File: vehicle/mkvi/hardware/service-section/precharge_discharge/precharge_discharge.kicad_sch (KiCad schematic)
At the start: 13 parts, among them J1 MicroFit_VT_5x1, J2 Automotive_M.2_Edge_Connector, K1 G2RG-2A-X_DC12, K2 3350-4275-126, Q1 SSM3K333R

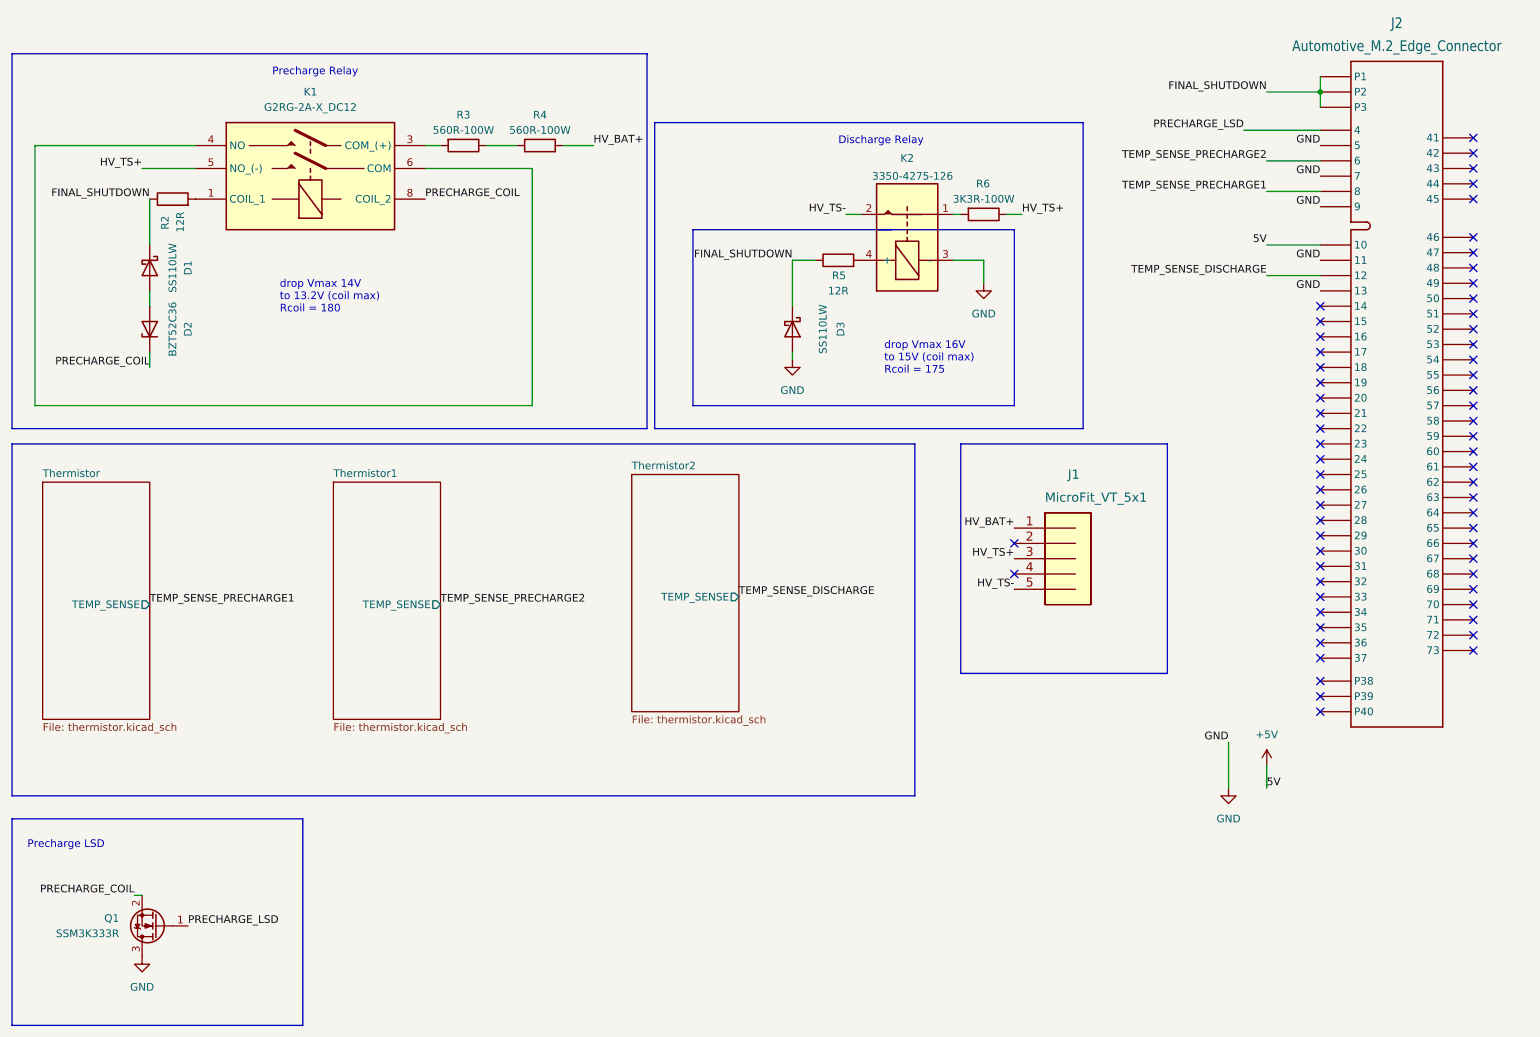
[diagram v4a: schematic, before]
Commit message: V3. Precharge_Discharge PCB Layout
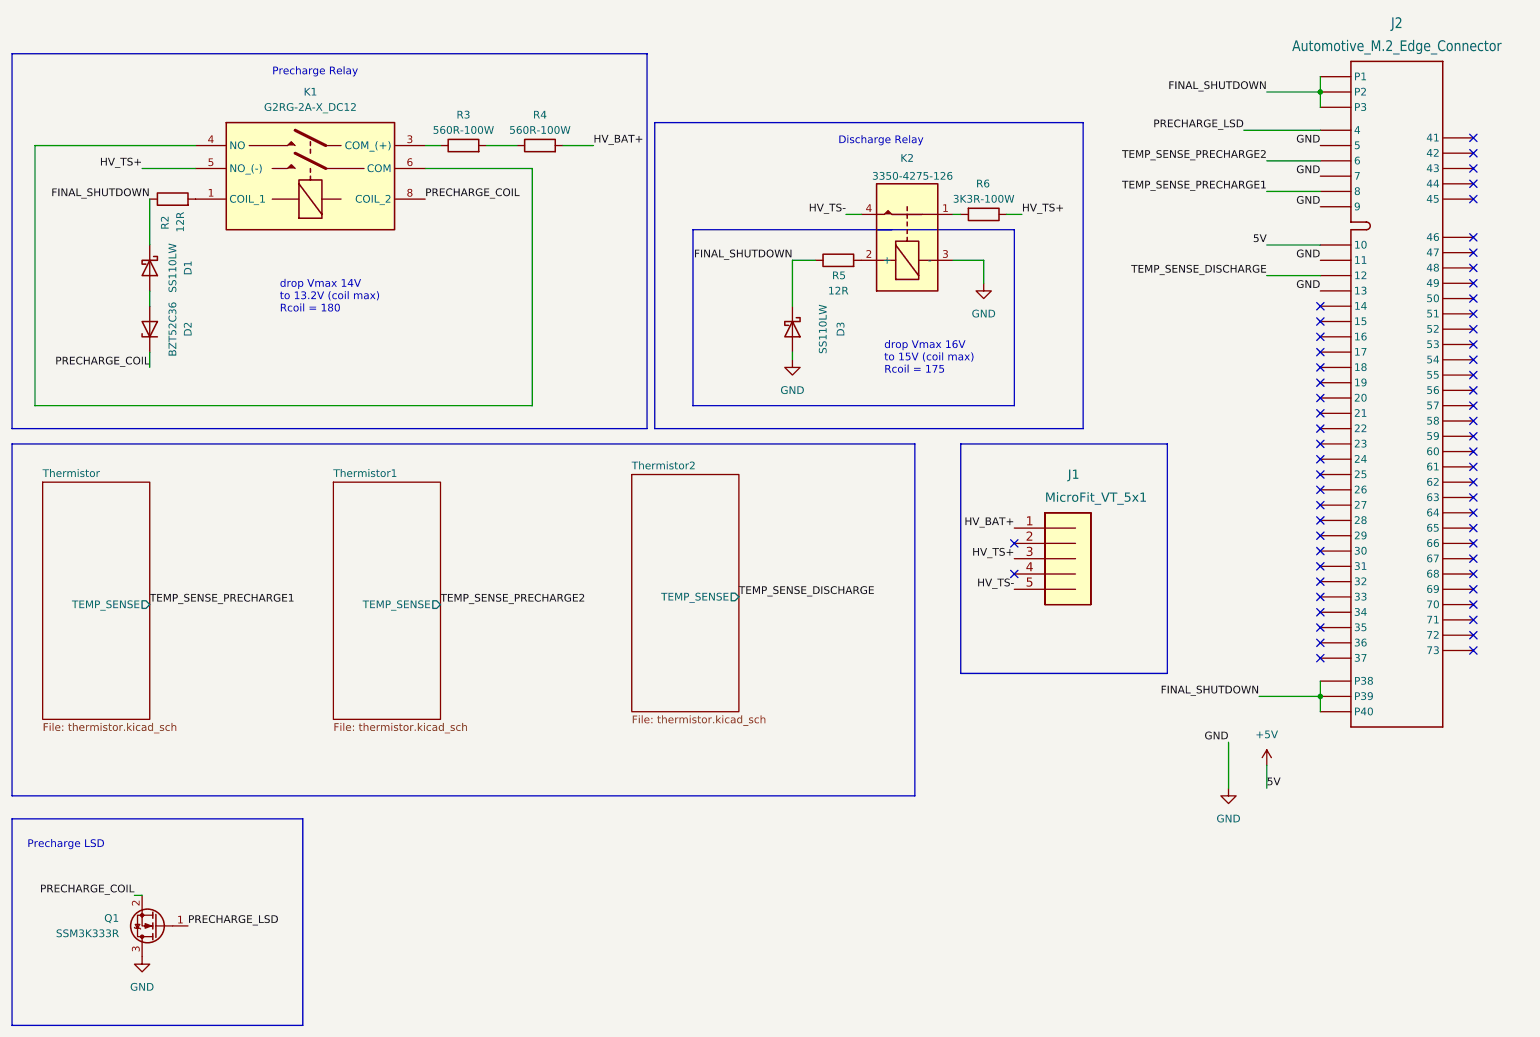
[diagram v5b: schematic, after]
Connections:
- net FINAL_SHUTDOWN: now also J2.P38, J2.P39, J2.P40
- net HV_TS-: now also K2.4; no longer K2.2
- net at K1.3 (COM_(+)): now also R3.1; no longer R3.2
- net at R5.2: now also K2.2 (+); no longer K2.4 (+)
- net at R4.1: now also R3.2; no longer R3.1
- no-connect marks 62 -> 59
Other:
- moved on the sheet: R3

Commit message: Implmeneted Requested Changes
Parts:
- added R1: R_10K, footprints:R_0805_OEM, symbol formula:R_10K
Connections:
- net GND: now also Q1.2 (S), R1.2; no longer Q1.3 (D)
- net PRECHARGE_COIL: now also Q1.3 (D); no longer Q1.2 (S)
- net PRECHARGE_LSD: now also R1.1
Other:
- moved on the sheet: Q1
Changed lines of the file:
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@@
+    (stroke (width 0) (type default) (color 0 0 0 0))
+  )
+  (wire (pts (xy 44.45 167.64) (xy 44.45 168.91))
     (stroke (width 0) (type default) (color 0 0 0 0))
   )
@@
     (stroke (width 0) (type default) (color 0 0 0 0))
   )
-  (wire (pts (xy 45.72 165.1) (xy 46.99 165.1))
+  (wire (pts (xy 50.8 162.56) (xy 52.07 162.56))
     (stroke (width 0) (type default) (color 0 0 0 0))
   )
@@
     (stroke (width 0) (type default) (color 0 0 0 0))
   )
+  (wire (pts (xy 52.07 176.53) (xy 52.07 172.72))
+    (stroke (width 0) (type default) (color 0 0 0 0))
+  )
   (polyline (pts (xy 73.66 152.4) (xy 25.4 152.4))
     (stroke (width 0) (type default) (color 0 0 0 0))
@@
     (effects (font (size 1.27 1.27)) (justify right bottom))
   )
-  (label "PRECHARGE_LSD" (at 54.61 170.18 0)
-    (effects (font (size 1.27 1.27)) (justify left bottom))
+  (label "PRECHARGE_LSD" (at 44.45 167.64 180)
+    (effects (font (size 1.27 1.27)) (justify right bottom))
   )
   (label "FINAL_SHUTDOWN" (at 48.26 49.53 180)
@@
     (effects (font (size 1.27 1.27)) (justify right bottom))
   )
-  (label "PRECHARGE_COIL" (at 45.72 165.1 180)
+  (label "PRECHARGE_COIL" (at 50.8 162.56 180)
     (effects (font (size 1.27 1.27)) (justify right bottom))
   )
@@
     (pin "2")
   )
-  (symbol (lib_id "power:GND") (at 46.99 175.26 0) (unit 1)
+  (symbol (lib_id "power:GND") (at 52.07 176.53 0) (unit 1)
     (in_bom yes) (on_board yes) (fields_autoplaced)
-    (property "Reference" "#PWR?" (id 0) (at 46.99 181.61 0)
-      (effects (font (size 1.27 1.27)) hide)
-    )
-    (property "Value" "GND" (id 1) (at 46.99 180.34 0))
-    (property "Footprint" "" (id 2) (at 46.99 175.26 0)
-      (effects (font (size 1.27 1.27)) hide)
-    )
-    (property "Datasheet" "" (id 3) (at 46.99 175.26 0)
+    (property "Reference" "#PWR?" (id 0) (at 52.07 182.88 0)
+      (effects (font (size 1.27 1.27)) hide)
+    )
+    (property "Value" "GND" (id 1) (at 52.07 181.61 0))
+    (property "Footprint" "" (id 2) (at 52.07 176.53 0)
+      (effects (font (size 1.27 1.27)) hide)
+    )
+    (property "Datasheet" "" (id 3) (at 52.07 176.53 0)
       (effects (font (size 1.27 1.27)) hide)
     )
@@
     (pin "1")
   )
-  (symbol (lib_id "OEM:SSM3K333R") (at 49.53 170.18 180) (unit 1)
+  (symbol (lib_id "OEM:SSM3K333R") (at 49.53 167.64 0) (unit 1)
     (in_bom yes) (on_board yes) (fields_autoplaced)
-    (property "Reference" "Q1" (id 0) (at 43.18 168.9099 0)
+    (property "Reference" "Q1" (id 0) (at 55.88 166.3699 0)
       (effects (font (size 1.27 1.27)) (justify left))
     )
-    (property "Value" "SSM3K333R" (id 1) (at 43.18 171.4499 0)
+    (property "Value" "SSM3K333R" (id 1) (at 55.88 168.9099 0)
       (effects (font (size 1.27 1.27)) (justify left))
     )
-    (property "Footprint" "OEM:SOT-23F" (id 2) (at 44.45 172.72 0)
-      (effects (font (size 1.27 1.27)) hide)
-    )
-    (property "Datasheet" "https://drive.google.com/file/d/1BgDITdtTCIIJgSi-AIzORLljOfl6uFKQ/view?usp=share_link" (id 3) (at 49.53 170.18 0)
-      (effects (font (size 1.27 1.27)) hide)
-    )
-    (property "MPN" "SSM3K333R,LF" (id 4) (at 43.18 172.7199 0)
+    (property "Footprint" "OEM:SOT-23F" (id 2) (at 54.61 165.1 0)
+      (effects (font (size 1.27 1.27)) hide)
+    )
+    (property "Datasheet" "https://drive.google.com/file/d/1BgDITdtTCIIJgSi-AIzORLljOfl6uFKQ/view?usp=share_link" (id 3) (at 49.53 167.64 0)
+      (effects (font (size 1.27 1.27)) hide)
+    )
+    (property "MPN" "SSM3K333R,LF" (id 4) (at 55.88 165.1001 0)
       (effects (font (size 1.27 1.27)) (justify left) hide)
     )
@@
     (property "MPN" "SS110LWRVGCT-ND" (id 5) (at 154.94 71.12 0)
       (effects (font (size 1.27 1.27)) hide)
+    )
+    (pin "1")
+    (pin "2")
+  )
+  (symbol (lib_id "formula:R_10K") (at 44.45 172.72 0) (unit 1)
+    (in_bom yes) (on_board yes)
+    (property "Reference" "R1" (id 0) (at 39.37 171.45 0)
+      (effects (font (size 1.27 1.27)) (justify left))
+    )
+    (property "Value" "R_10K" (id 1) (at 36.83 173.99 0)
+      (effects (font (size 1.27 1.27)) (justify left))
+    )
+    (property "Footprint" "footprints:R_0805_OEM" (id 2) (at 42.672 172.72 0)
+      (effects (font (size 1.27 1.27)) hide)
+    )
+    (property "Datasheet" "http://www.bourns.com/data/global/pdfs/CRS.pdf" (id 3) (at 46.482 172.72 0)
+      (effects (font (size 1.27 1.27)) hide)
+    )
+    (property "MFN" "DK" (id 4) (at 44.45 172.72 0)
+      (effects (font (size 1.524 1.524)) hide)
+    )
+    (property "MPN" "CRS0805-FX-1002ELFCT-ND" (id 5) (at 44.45 172.72 0)
+      (effects (font (size 1.524 1.524)) hide)
+    )
+    (property "PurchasingLink" "https://www.digikey.com/products/en?keywords=CRS0805-FX-1002ELFCT-ND" (id 6) (at 56.642 162.56 0)
+      (effects (font (size 1.524 1.524)) hide)
     )
     (pin "1")
@@
     (pin "2")
   )
+  (symbol (lib_id "power:GND") (at 44.45 176.53 0) (unit 1)
+    (in_bom yes) (on_board yes) (fields_autoplaced)
+    (property "Reference" "#PWR?" (id 0) (at 44.45 182.88 0)
+      (effects (font (size 1.27 1.27)) hide)
+    )
+    (property "Value" "GND" (id 1) (at 44.45 181.61 0))
+    (property "Footprint" "" (id 2) (at 44.45 176.53 0)
+      (effects (font (size 1.27 1.27)) hide)
+    )
+    (property "Datasheet" "" (id 3) (at 44.45 176.53 0)
+      (effects (font (size 1.27 1.27)) hide)
+    )
+    (pin "1")
+  )
   (symbol (lib_id "OEM:560R-100W") (at 113.03 40.64 90) (unit 1)
     (in_bom yes) (on_board yes)
@@
       (reference "#PWR?") (unit 1) (value "GND") (footprint "")
     )
+    (path "/cc5bfc57-2f12-4c76-8ed2-02c6ef8ddcaa"
+      (reference "#PWR?") (unit 1) (value "GND") (footprint "")
+    )
     (path "/1d3603a0-934c-404e-9b38-4b65044f588c/6dc3a5a5-6ba7-45ee-890e-2b247ac5cbfa"
       (reference "C1") (unit 1) (value "C_10nF") (footprint "OEM:C_0603")
@@
       (reference "Q1") (unit 1) (value "SSM3K333R") (footprint "OEM:SOT-23F")
     )
+    (path "/929c2eb8-8f4f-4761-a95e-9e5a48d04631"
+      (reference "R1") (unit 1) (value "R_10K") (footprint "footprints:R_0805_OEM")
+    )
     (path "/bded9724-57bc-420a-b565-6c39cf6fe6c3"

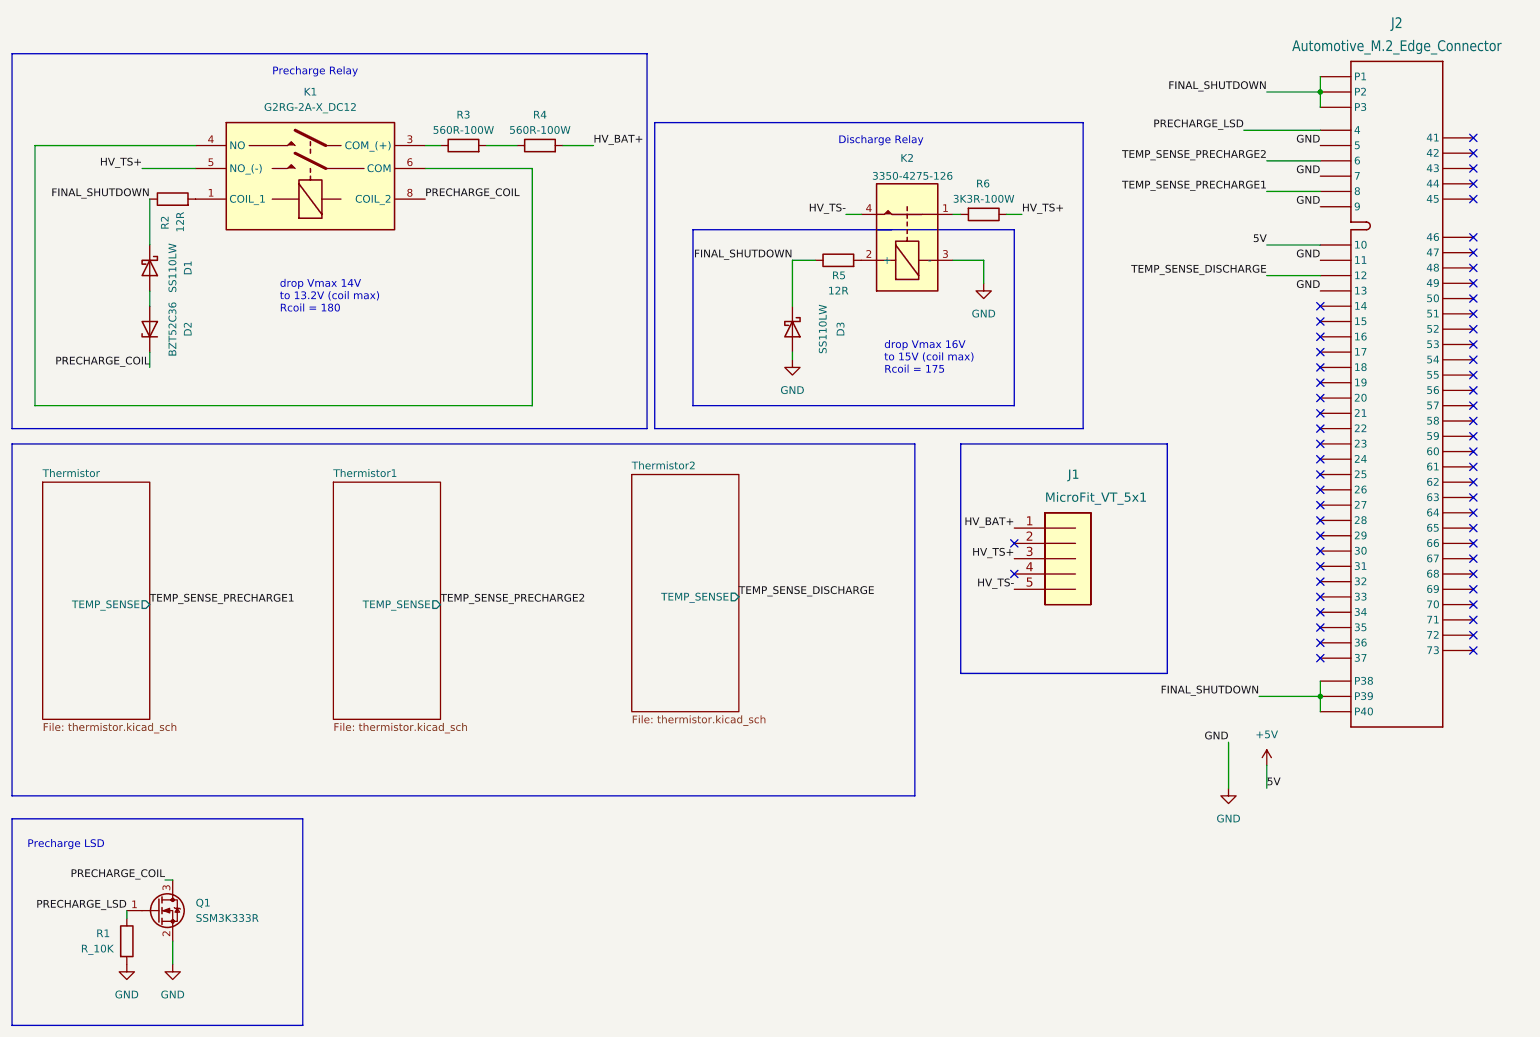
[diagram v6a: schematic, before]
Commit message: fix drc warnings
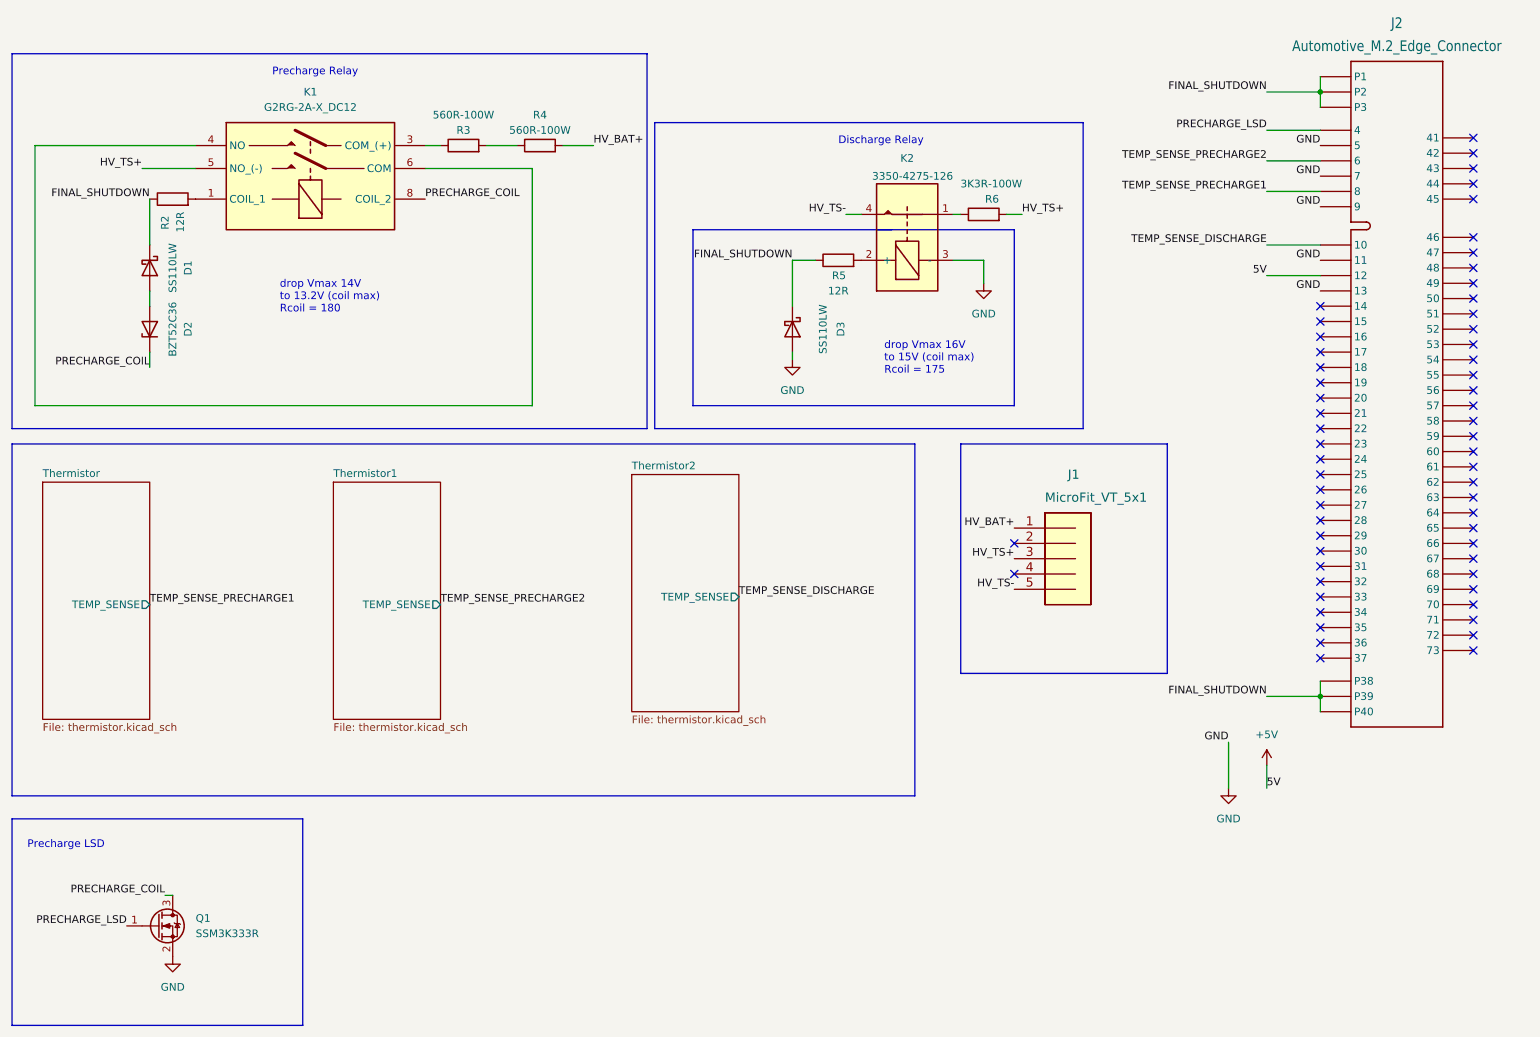
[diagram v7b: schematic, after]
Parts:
- removed R1: R_10K, footprints:R_0805_OEM, symbol formula:R_10K
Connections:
- net +5V: now also J2.12; no longer J2.10
- net HV_TS+: now also R6.2; no longer R6.1
- net TEMP_SENSE_DISCHARGE: now also J2.10; no longer J2.12
- net at K2.1: now also R6.1; no longer R6.2
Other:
- moved on the sheet: Q1, R6
